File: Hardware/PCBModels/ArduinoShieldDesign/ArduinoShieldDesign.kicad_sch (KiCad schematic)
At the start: 2 parts, among them J1 Conn_01x04_Socket

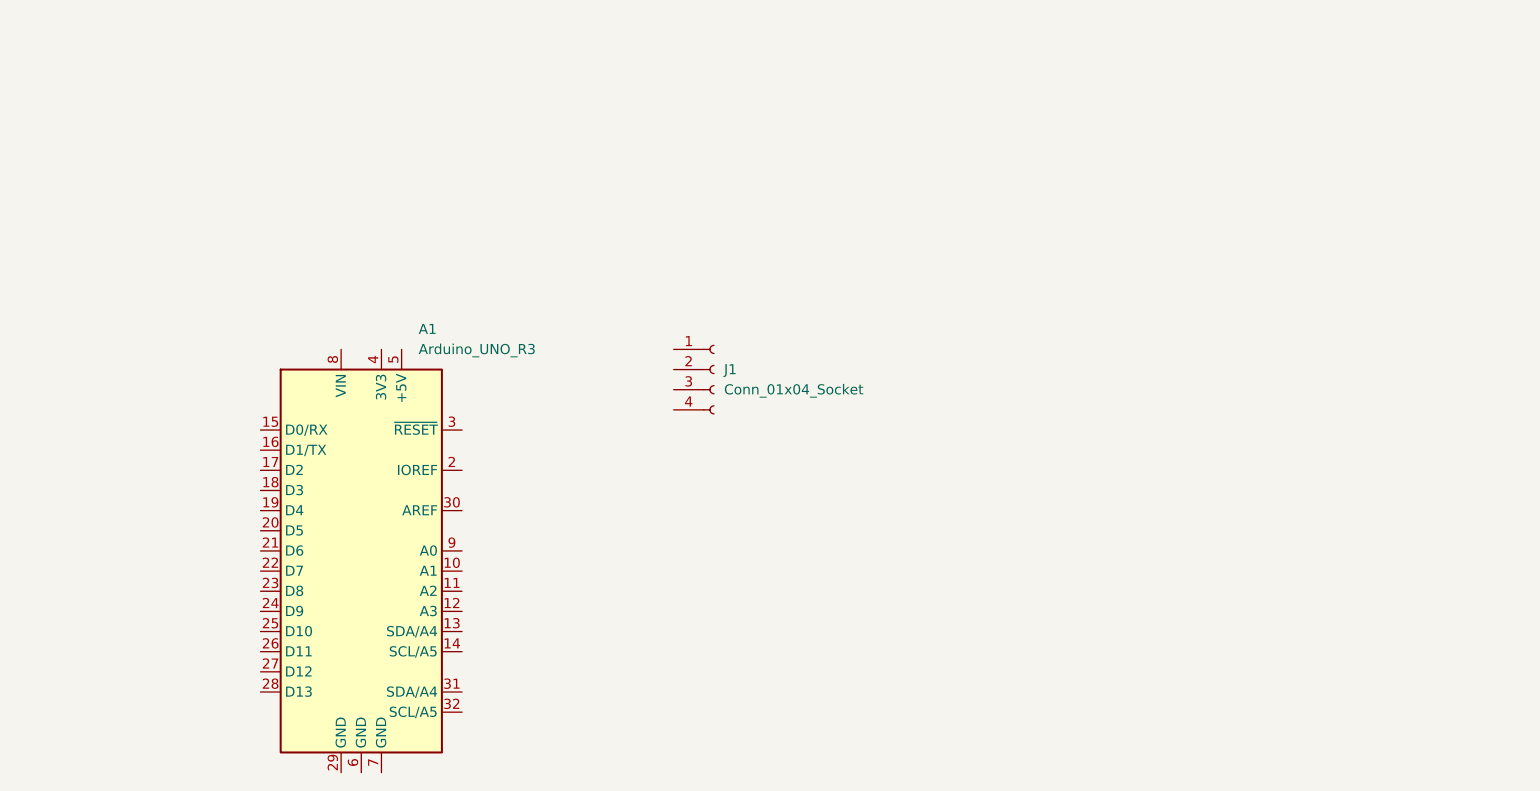
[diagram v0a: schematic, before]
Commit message: Working on the PCB Design and an updated Encoder count
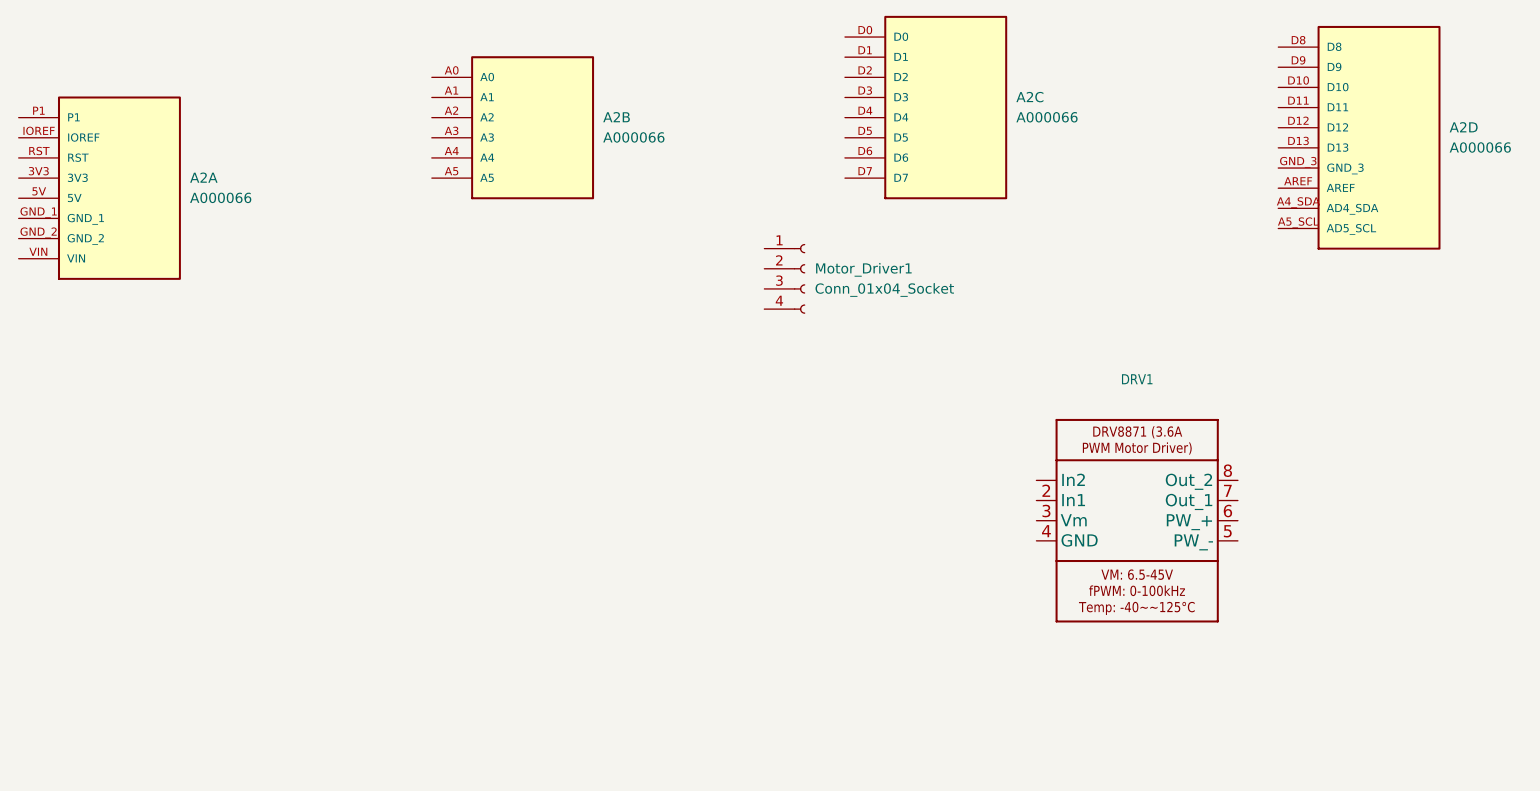
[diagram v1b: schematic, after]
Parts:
- removed A1: Arduino_UNO_R3, Module:Arduino_UNO_R3, symbol MCU_Module:Arduino_UNO_R3
- added A2: A000066, A000066:ARDUINO_A000066, symbol CEWBArduinoUnoR3:A000066
- added DRV1: ~, DRV8871_driver(1):DRV8871_manual, symbol AdafruitDRV8871DriverBreakout:DRV8871_manual
- renumbered J1 to Motor_Driver1
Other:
- moved on the sheet: Motor_Driver1
